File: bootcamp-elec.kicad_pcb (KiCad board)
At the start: 2 copper layers, 23.1 x 32 mm, 18 parts, among them J3 FTDI, SW1 SW_Push, U1 ATmega328P-A, Y1 16MHz

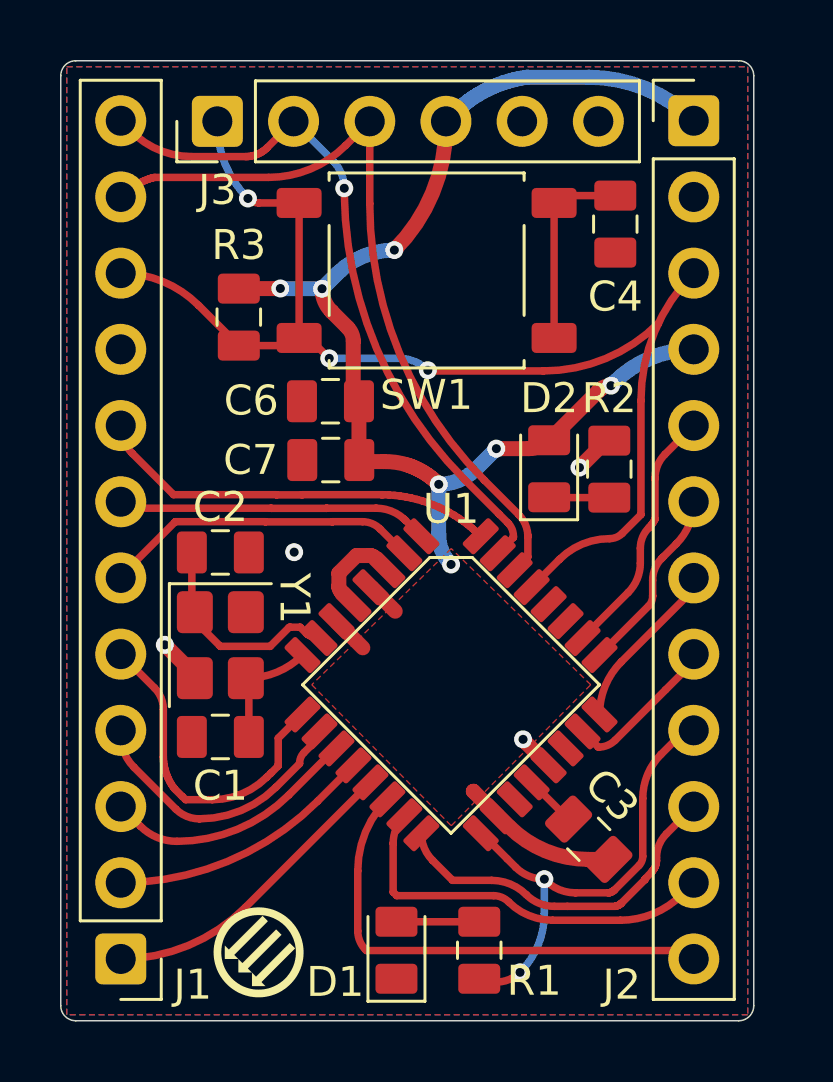
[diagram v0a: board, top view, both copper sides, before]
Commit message: move footprints
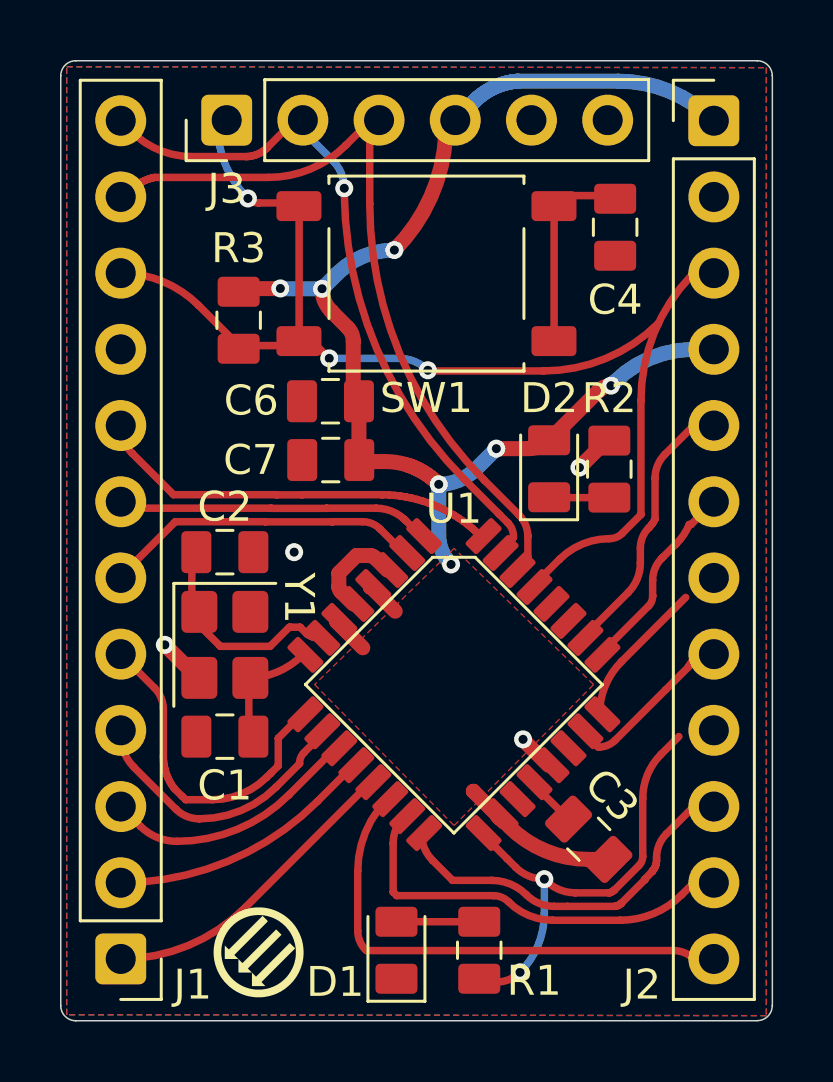
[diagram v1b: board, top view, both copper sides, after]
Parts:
- moved J2 0.67 mm to (109.8, 47.0)
- moved J3 0.31 mm to (93.5, 47.0)
- moved C1 0.15 mm to (93.5, 67.5)
- moved Y1 0.15 mm to (93.5, 64.5)
- moved C2 0.15 mm to (93.5, 61.4)
- moved C4 0.11 mm to (106.5, 50.5)
- moved R3 0.11 mm to (93.9, 53.6)
- moved SW1 0.11 mm to (100.2, 52.1)
- moved U1 0.10 mm to (101.1, 65.8)
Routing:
- net A0: track 5.71 -> 6.88 mm
- net DTR: track 41.6 -> 42.8 mm
- net D10: track 16.3 -> 17.0 mm
- net MOSI: track 13.5 -> 14.2 mm
- net A3: track 8.51 -> 9.18 mm
- net MISO: track 12.0 -> 12.6 mm
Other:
- board size 23.1 x 32 mm -> 23.7 x 32 mm

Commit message: pcb_design 4.0
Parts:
- moved G*** 3.35 mm to (97.3, 72.7)
- moved D1 1.93 mm to (97.5, 75.6), turned to 0 degrees
- moved R1 1.36 mm to (101.0, 75.7), turned to 0 degrees
- moved C3 1.08 mm to (104.5, 70.9), turned to 45 degrees
- moved D2 1.03 mm to (104.5, 57.6)
- moved R2 1.03 mm to (106.6, 57.6)
- moved J2 0.67 mm to (109.1, 47.0)
- moved R3 0.38 mm to (93.9, 53.3)
- moved J3 0.31 mm to (93.2, 47.0)
- moved C1 0.15 mm to (93.3, 67.5)
- moved Y1 0.15 mm to (93.3, 64.5)
- moved C2 0.15 mm to (93.3, 61.4)
- moved C4 0.14 mm to (106.5, 50.7)
- moved SW1 0.12 mm to (100.2, 52.0)
- moved U1 0.10 mm to (101.0, 65.8)
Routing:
- net DTR: track 42.8 -> 38.8 mm
- net RAW: track 50.2 -> 46.4 mm, vias 7 -> 5
- net D10: track 17.0 -> 13.8 mm
- net GND: track 7.39 -> 4.29 mm
- net MOSI: track 14.2 -> 12.4 mm
- net A0: track 6.88 -> 5.27 mm
- net MISO: track 12.6 -> 11.2 mm
- net Net-(D1-Pad2): track 2.76 -> 1.62 mm
- net A3: track 9.18 -> 8.24 mm
- net D2: track 13.8 -> 12.9 mm
- net SCK: track 15.9 -> 15.1 mm
- net TXO: track 24.0 -> 23.5 mm, vias 1 -> 0
- net RXI: track 26.5 -> 26.1 mm, vias 0 -> 1
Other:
- board size 23.7 x 32 mm -> 23.1 x 32 mm
